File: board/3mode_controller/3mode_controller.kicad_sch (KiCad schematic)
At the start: 34 parts, among them IC1 DW01A, J1 JST XH, J2 USB_C_Receptacle, Q1 FDN336P, SW1 reset, SW2 ChangeScreen, SW2 boot, SW4 SW_SPDT, U1 TP4056, U2 ESP32-S3-WROOM-1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

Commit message: schematic finished
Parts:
- removed J1: JST XH, Connector_JST:JST_PH_S2B-PH-K_1x02_P2.00mm_Horizontal, symbol Connector:Conn_01x02_Socket
- added C2: 10u, Capacitor_SMD:C_0603_1608Metric_Pad1.08x0.95mm_HandSolder, symbol Device:C
- added C7, C8: 10u, Capacitor_Tantalum_SMD:CP_EIA-3216-18_Kemet-A_Pad1.58x1.35mm_HandSolder, symbol Device:C
- added J1: Conn_01x04_Socket, symbol Connector:Conn_01x04_Socket
- added R17 (x2): 5.1K, Resistor_SMD:R_0603_1608Metric_Pad0.98x0.95mm_HandSolder, symbol Device:R
- added U6: NRF24L01_Breakout, RF_Module:nRF24L01_Breakout, symbol RF:NRF24L01_Breakout
- SW2: footprint Button_Switch_SMD:SW_SPST_CK_RS282G05A3 -> Button_Switch_THT:SW_PUSH_6mm
- SW4: footprint (none) -> Button_Switch_THT:SW_Slide_1P2T_CK_OS102011MS2Q; LCSC (none) -> C431548
- U5: LCSC (none) -> C2992570
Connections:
- net +3.3V: now also C8.1, J1.2 (Pin_2), R17.1, R17.1, U6.2 (VCC)
- net +5V: now also D2.2 (A), D3.2 (A)
- net GND: now also SW2.2, C2.2, C7.2, C8.2, J1.1 (Pin_1), U6.1 (GND)
- net VBUS: no longer D2.2 (A), D3.2 (A)
- net at SW4.3 (C), U5.3 (VI): now also C7.1
- net ESP32_BUTTON: now reaches SW2.1
- net ESP32_BUTTON: now also U2.5 (GPIO5/TOUCH5/ADC1_CH4), C2.1
- net ESP32_SCREEN_SCK: now reaches U2.12 (GPIO8/TOUCH8/ADC1_CH7/SUBSPICS1)
- net ESP32_SCREEN_SCK: now also J1.3 (Pin_3), R17.2
- net ESP32_SCREEN_SDA: now reaches U2.17 (GPIO9/TOUCH9/ADC1_CH8/FSPIHD/SUBSPIHD)
- net ESP32_SCREEN_SDA: now also J1.4 (Pin_4), R17.2
- net ESP32_RF_SPI_CNS: now reaches U2.18 (GPIO10/TOUCH10/ADC1_CH9/FSPICS0/FSPIIO4/SUBSPICS0)
- net ESP32_RF_SPI_CNS: now also U6.4 (~{CSN})
- net ESP32_RF_SPI_MOSI: now reaches U2.19 (GPIO11/TOUCH11/ADC2_CH0/FSPID/FSPIIO5/SUBSPID)
- net ESP32_RF_SPI_MOSI: now also U6.6 (MOSI)
- net ESP32_RF_SPI_SCK: now reaches U2.20 (GPIO12/TOUCH12/ADC2_CH1/FSPICLK/FSPIIO6/SUBSPICLK)
- net ESP32_RF_SPI_SCK: now also U6.5 (SCK)
- net ESP32_RF_SPI_MISO: now reaches U2.21 (GPIO13/TOUCH13/ADC2_CH2/FSPIQ/FSPIIO7/SUBSPIQ)
- net ESP32_RF_SPI_MISO: now also U6.7 (MISO)
- net ESP32_JOYSTICK_X: now reaches U2.38 (GPIO2/TOUCH2/ADC1_CH1)
- net ESP32_JOYSTICK_Y: now reaches U2.39 (GPIO1/TOUCH1/ADC1_CH0)
- net ESP32_RF_SPI_CE: now reaches U2.4 (GPIO4/TOUCH4/ADC1_CH3)
- net ESP32_RF_SPI_CE: now also U6.3 (CE)
- no-connect marks 41 -> 38
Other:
- moved on the sheet: D3, H1, H2, J2, R17, R4, R7, SW2, SW4, U5

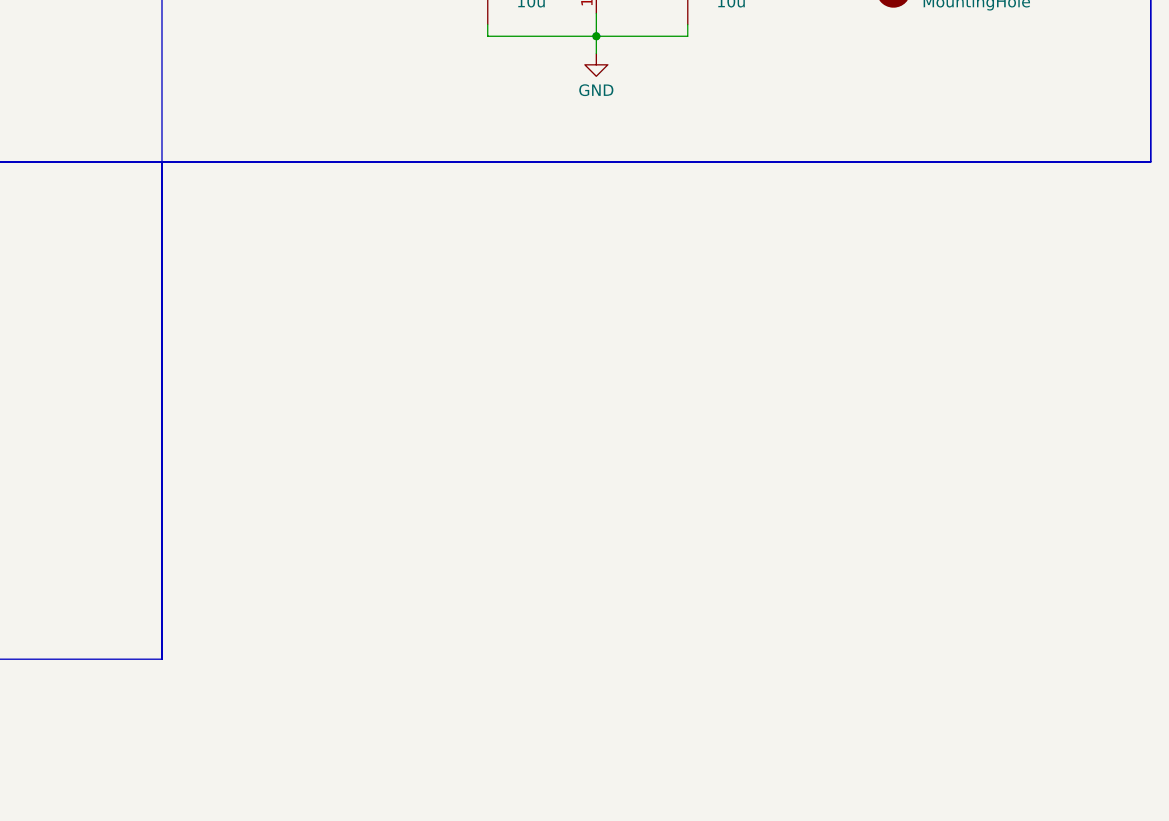
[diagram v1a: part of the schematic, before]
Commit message: added the joysticks to the schematic
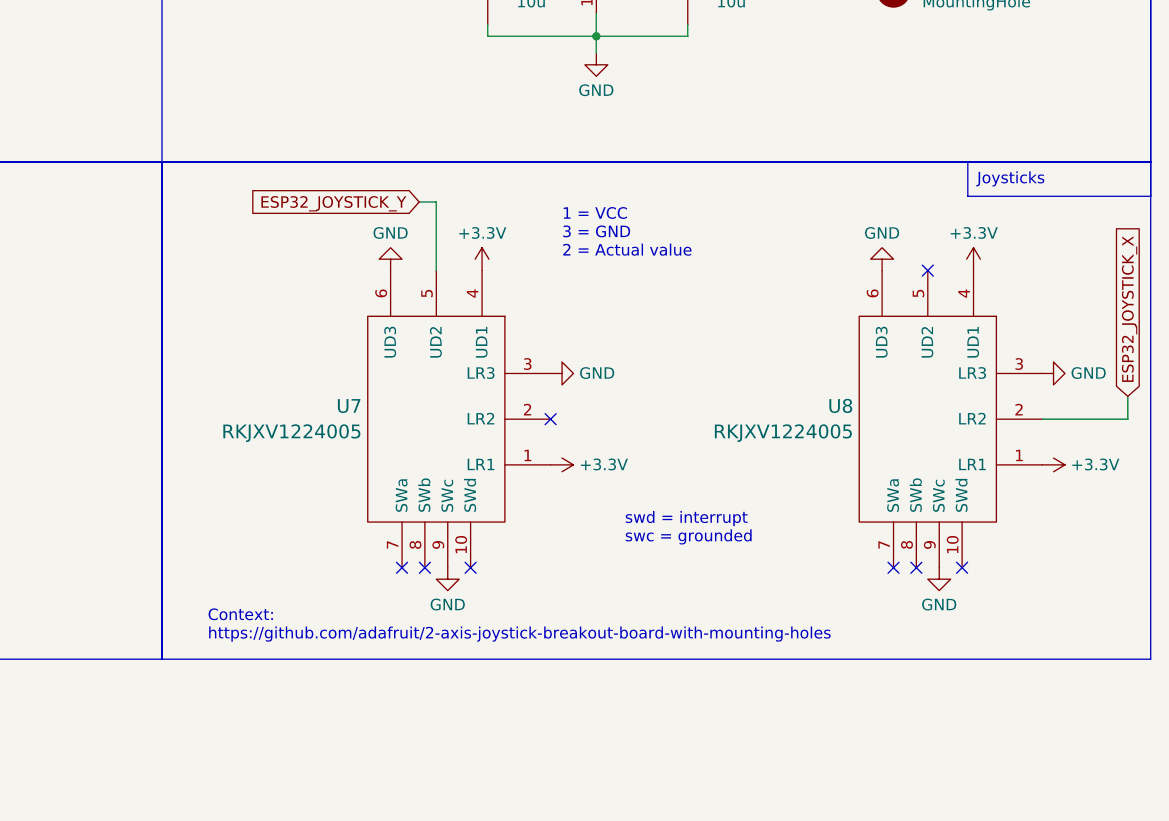
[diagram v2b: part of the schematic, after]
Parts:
- added U7, U8: RKJXV1224005, kicad-lib-input:RKJXV1224005, symbol joystick:RKJXV1224005
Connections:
- net +3.3V: now also U7.1 (LR1), U7.4 (UD1), U8.1 (LR1), U8.4 (UD1)
- net ESP32_JOYSTICK_X: now also U8.2 (LR2)
- net ESP32_JOYSTICK_Y: now also U7.5 (UD2)
- net GND: now also U7.3 (LR3), U7.6 (UD3), U7.9 (SWc), U8.3 (LR3), U8.6 (UD3), U8.9 (SWc)
- no-connect marks 38 -> 46
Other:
- note added: "1 = VCC 3 = GND 2 = Actual value"
- note added: "Context: https://github.com/adafruit/2-axis-joystick-breakout-board-with-mounting-holes"
- note added: "swd = interrupt swc = grounded"

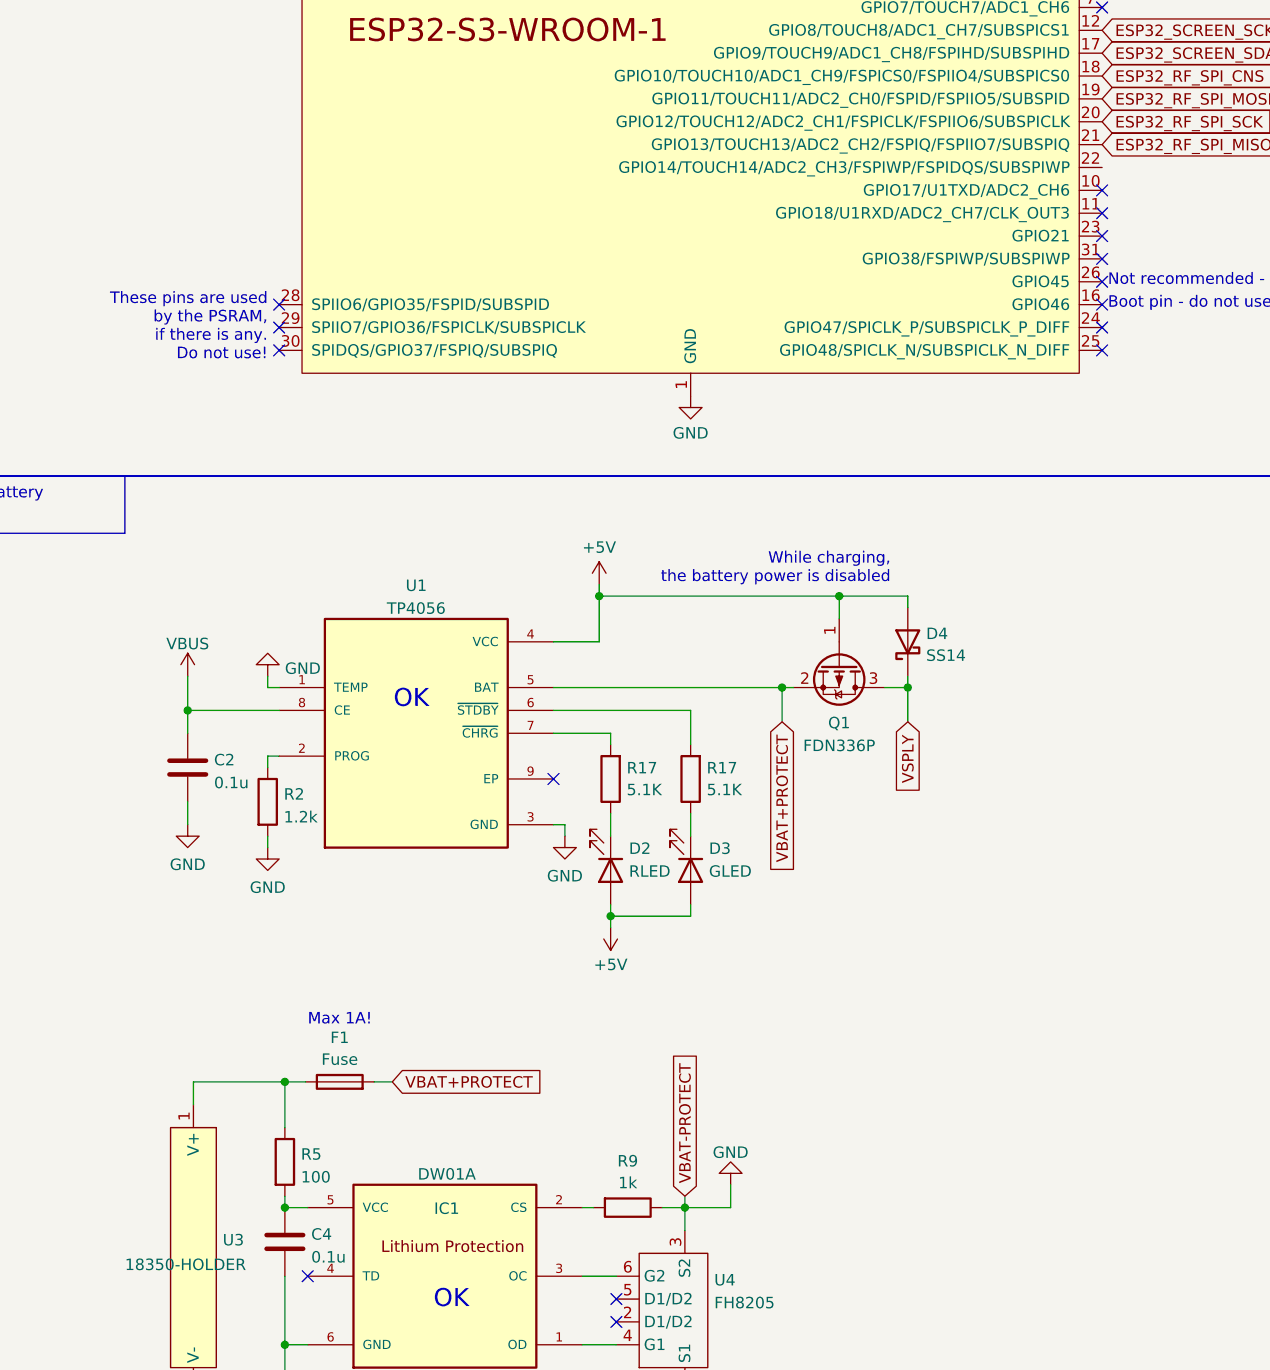
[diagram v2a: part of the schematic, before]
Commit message: added symbols and footprints for the battery charging ICs
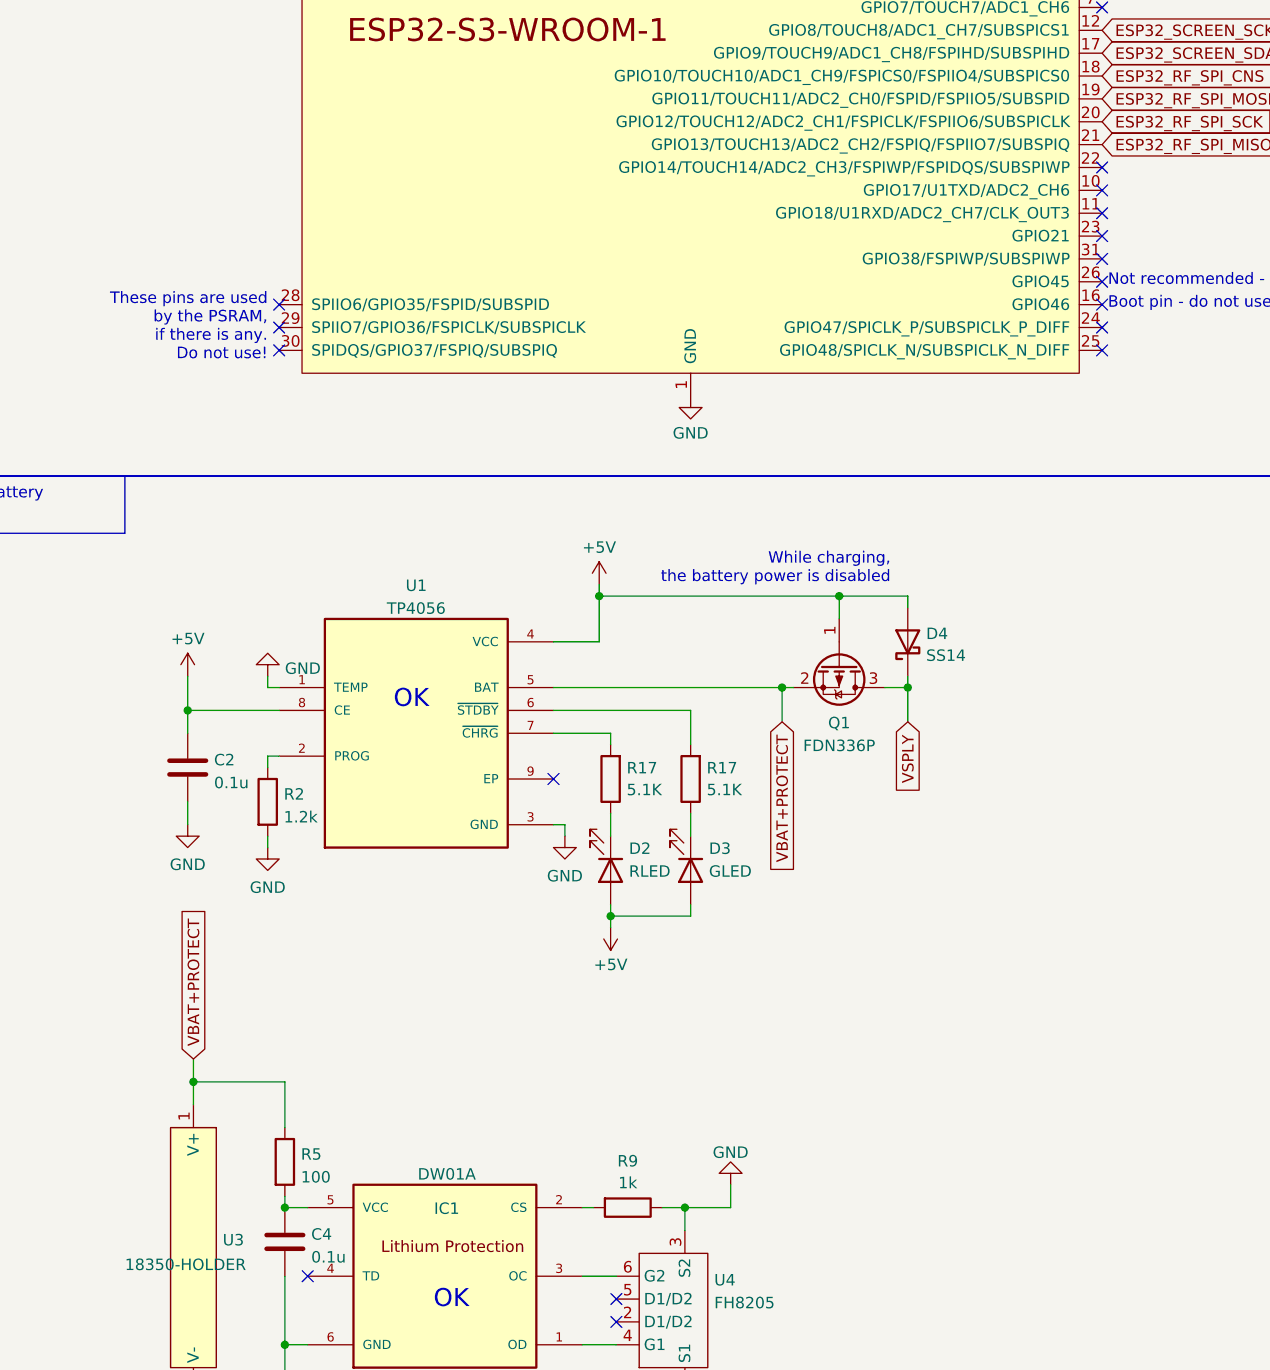
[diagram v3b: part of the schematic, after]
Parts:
- removed F1: Fuse, Fuse:Fuse_0603_1608Metric_Pad1.05x0.95mm_HandSolder, symbol Device:Fuse
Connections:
- net VBUS is gone; now on net +5V: C2.1, U1.8 (CE)
- net VBAT+PROTECT: now also R5.1, U3.1 (V+)
- no-connect marks 46 -> 47
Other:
- note removed: "Max 1A!"
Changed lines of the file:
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@@
   (junction (at 327.66 34.29) (diameter 0) (color 0 0 0 0)
   )
+  (junction (at 39.37 197.485) (diameter 0) (color 0 0 0 0)
+  )
   (junction (at 38.735 156.21) (diameter 0) (color 0 0 0 0)
   )
@@
   )
   (junction (at 290.195 44.45) (diameter 0) (color 0 0 0 0)
-  )
-  (junction (at 49.53 197.485) (diameter 0) (color 0 0 0 0)
   )
   (no_connect (at 215.265 75.565))
@@
   (no_connect (at 215.265 90.805))
   (no_connect (at 215.265 93.345))
+  (no_connect (at 140.335 95.885))
   (no_connect (at 48.895 111.125))
   (no_connect (at 354.965 175.26))
@@
   (no_connect (at 140.335 78.105))
   (no_connect (at 48.895 65.405))
-  (wire (pts (xy 49.53 197.485) (xy 51.816 197.485))
-    (stroke (width 0) (type default))
-  )
   (wire (pts (xy 116.205 153.67) (xy 118.745 153.67))
     (stroke (width 0) (type default))
@@
     (stroke (width 0) (type default))
   )
-  (wire (pts (xy 59.436 197.485) (xy 61.468 197.485))
-    (stroke (width 0) (type default))
-  )
   (wire (pts (xy 48.895 45.085) (xy 41.275 45.085))
     (stroke (width 0) (type default))
@@
     (stroke (width 0) (type default))
   )
+  (wire (pts (xy 39.37 194.945) (xy 39.37 197.485))
+    (stroke (width 0) (type default))
+  )
   (wire (pts (xy 232.41 47.625) (xy 224.79 47.625))
     (stroke (width 0) (type default))
@@
   )
   (wire (pts (xy 330.2 54.61) (xy 325.12 54.61))
-    (stroke (width 0) (type default))
-  )
-  (wire (pts (xy 93.98 210.185) (xy 93.98 211.455))
     (stroke (width 0) (type default))
   )
@@
     (fill (type none))
     (effects (font (size 1.27 1.27)) (justify left top))
-  )
-  (text "Max 1A!" (at 52.07 191.389 0)
-    (effects (font (size 1.27 1.27)) (justify left bottom))
   )
   (text "1 = VCC\n3 = GND\n2 = Actual value" (at 318.135 140.97 0)
@@
     )
   )
-  (global_label "VBAT+PROTECT" (shape input) (at 61.468 197.485 0) (fields_autoplaced)
+  (global_label "VBAT+PROTECT" (shape input) (at 39.37 194.945 90) (fields_autoplaced)
     (effects (font (size 1.27 1.27)) (justify left))
-    (property "Intersheetrefs" "${INTERSHEET_REFS}" (at 78.6651 197.485 0)
+    (property "Intersheetrefs" "${INTERSHEET_REFS}" (at 39.37 177.7479 90)
       (effects (font (size 1.27 1.27)) (justify left) hide)
     )
@@
     )
   )
-  (global_label "VBAT-PROTECT" (shape input) (at 93.98 210.185 90) (fields_autoplaced)
-    (effects (font (size 1.27 1.27)) (justify left))
-    (property "Intersheetrefs" "${INTERSHEET_REFS}" (at 93.9006 193.56 90)
-      (effects (font (size 1.27 1.27)) (justify left) hide)
-    )
-  )
   (global_label "ESP32_RF_SPI_SCK" (shape input) (at 212.725 154.305 180) (fields_autoplaced)
     (effects (font (size 1.27 1.27)) (justify right))
@@
         (path "/9c1091b5-dc9c-4275-a62f-af3d6f92e0db"
           (reference "#PWR0111") (unit 1)
-        )
-      )
-    )
-  )
-  (symbol (lib_id "Device:Fuse") (at 55.626 197.485 90) (unit 1)
-    (in_bom yes) (on_board yes) (dnp no) (fields_autoplaced)
-    (property "Reference" "F1" (at 55.626 192.5787 90)
-      (effects (font (size 1.27 1.27)))
-    )
-    (property "Value" "Fuse" (at 55.626 195.0029 90)
-      (effects (font (size 1.27 1.27)))
-    )
-    (property "Footprint" "Fuse:Fuse_0603_1608Metric_Pad1.05x0.95mm_HandSolder" (at 55.626 199.263 90)
-      (effects (font (size 1.27 1.27)) hide)
-    )
-    (property "Datasheet" "https://www.lcsc.com/product-detail/Fuses_Shenzhen-lanson-Elec-06H1100D_C182303.html" (at 55.626 197.485 0)
-      (effects (font (size 1.27 1.27)) hide)
-    )
-    (property "LCSC" "C182303" (at 55.626 197.485 90)
-      (effects (font (size 1.27 1.27)) hide)
-    )
-    (pin "1")
-    (pin "2")
-    (instances
-      (project "3mode_controller"
-        (path "/64deb2d4-0f1e-4037-b447-7d4c34ae11e6"
-          (reference "F1") (unit 1)
-        )
-      )
-      (project "smoke_extractorV1_1"
-        (path "/9c1091b5-dc9c-4275-a62f-af3d6f92e0db"
-          (reference "F1") (unit 1)
         )
       )
@@
         (path "/64deb2d4-0f1e-4037-b447-7d4c34ae11e6"
           (reference "#PWR04") (unit 1)
+        )
+      )
+    )
+  )
+  (symbol (lib_id "power:+5V") (at 38.735 152.4 0) (unit 1)
+    (in_bom yes) (on_board yes) (dnp no) (fields_autoplaced)
+    (property "Reference" "#PWR012" (at 38.735 156.21 0)
+      (effects (font (size 1.27 1.27)) hide)
+    )
+    (property "Value" "+5V" (at 38.735 148.2669 0)
+      (effects (font (size 1.27 1.27)))
+    )
+    (property "Footprint" "" (at 38.735 152.4 0)
+      (effects (font (size 1.27 1.27)) hide)
+    )
+    (property "Datasheet" "" (at 38.735 152.4 0)
+      (effects (font (size 1.27 1.27)) hide)
+    )
+    (pin "1")
+    (instances
+      (project "3mode_controller"
+        (path "/64deb2d4-0f1e-4037-b447-7d4c34ae11e6"
+          (reference "#PWR012") (unit 1)
         )
       )
@@
         )
       )
-    )
-  )
-  (symbol (lib_id "power:VBUS") (at 38.735 152.4 0) (unit 1)
-    (in_bom yes) (on_board yes) (dnp no) (fields_autoplaced)
-    (property "Reference" "#PWR012" (at 38.735 156.21 0)
-      (effects (font (size 1.27 1.27)) hide)
-    )
-    (property "Value" "VBUS" (at 38.735 148.8242 0)
-      (effects (font (size 1.27 1.27)))
-    )
-    (property "Footprint" "" (at 38.735 152.4 0)
-      (effects (font (size 1.27 1.27)) hide)
-    )
-    (property "Datasheet" "" (at 38.735 152.4 0)
-      (effects (font (size 1.27 1.27)) hide)
-    )
-    (pin "1")
-    (instances
-      (project "3mode_controller"
-        (path "/64deb2d4-0f1e-4037-b447-7d4c34ae11e6"
-          (reference "#PWR012") (unit 1)
-        )
-      )
-      (project "smoke_extractorV1_1"
-        (path "/9c1091b5-dc9c-4275-a62f-af3d6f92e0db"
-          (reference "#PWR0106") (unit 1)
-        )
-      )
